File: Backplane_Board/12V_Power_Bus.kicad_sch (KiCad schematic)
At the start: 17 parts, among them U5 PKU3511SPI

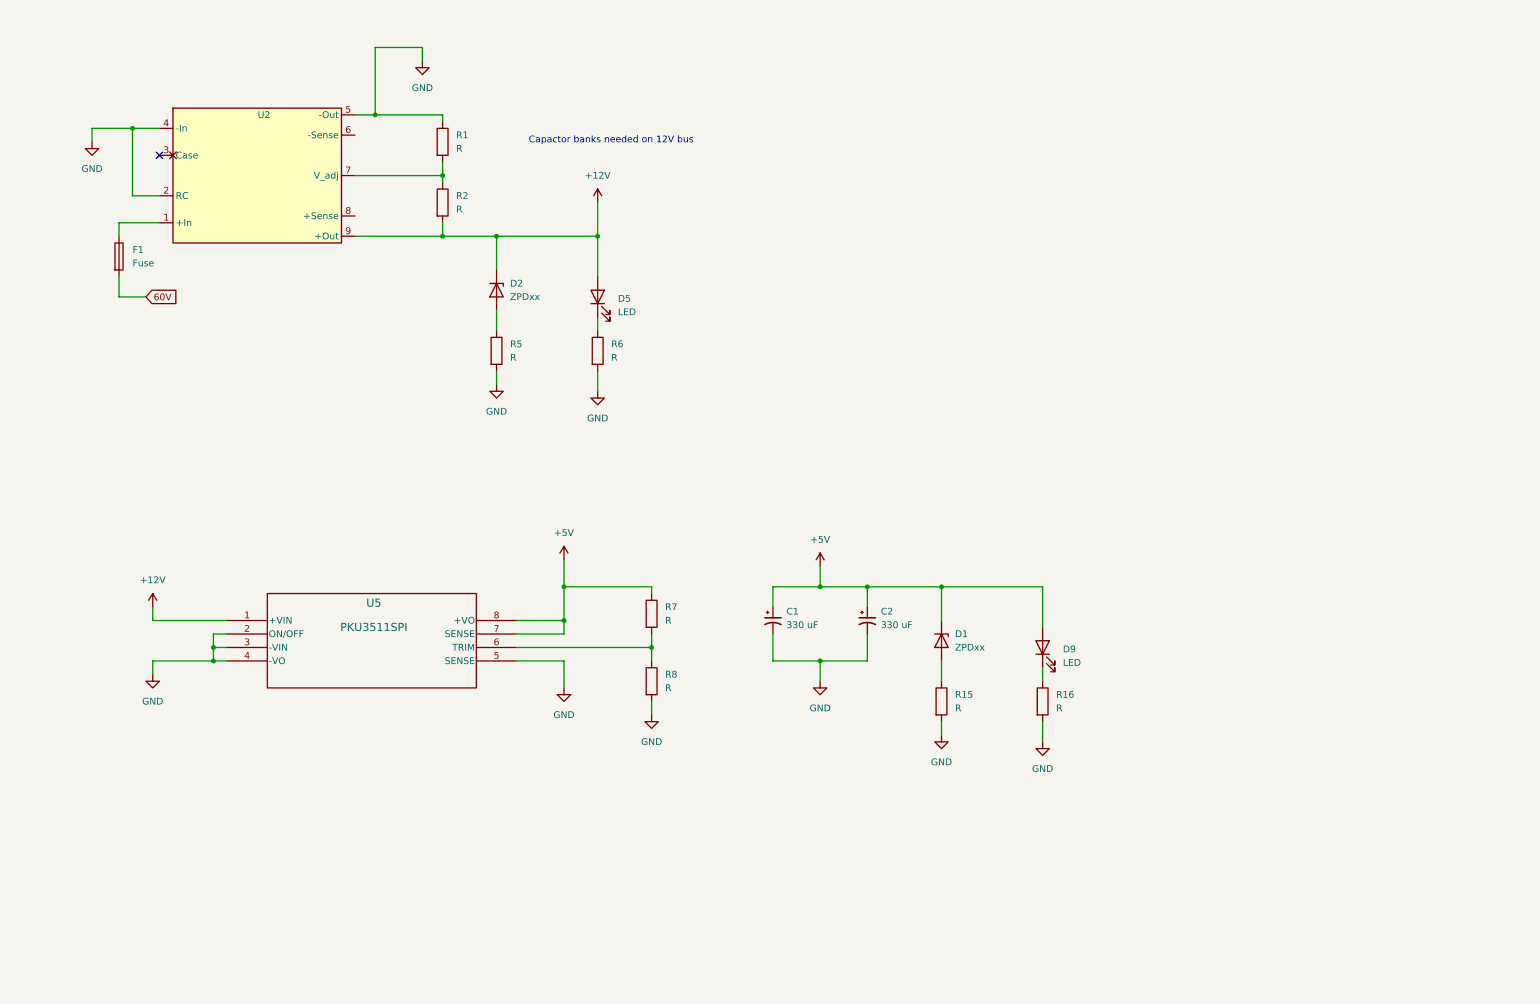
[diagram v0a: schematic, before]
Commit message: added ad converter
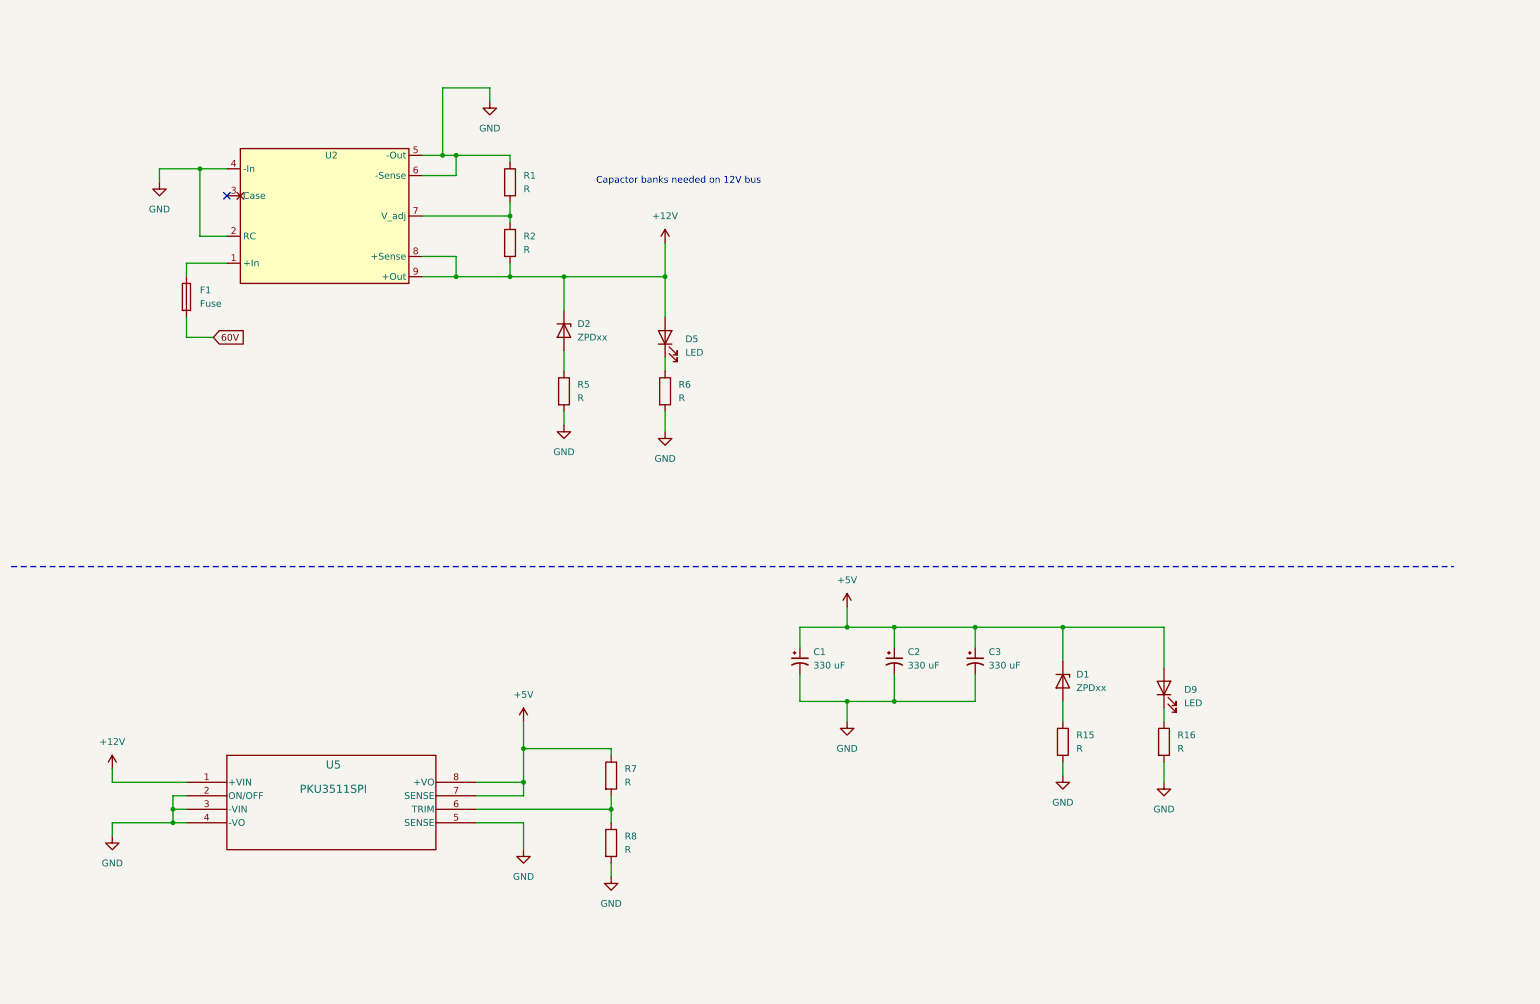
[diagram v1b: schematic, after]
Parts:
- added C3: 330 uF, 220UF CAP:CAP_16SVPG330MX, symbol Device:C_Polarized_Small_US
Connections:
- net +12V: now also U2.8 (+Sense)
- net +5V: now also C3.1
- net GND: now also U2.6 (-Sense), C3.2
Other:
- moved on the sheet: C1, C2, D1, D2, D5, D9, F1, R1, R15, R16, R2, R5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

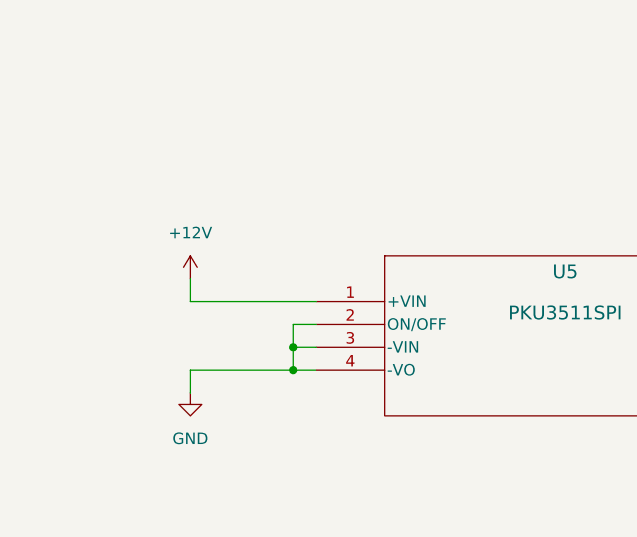
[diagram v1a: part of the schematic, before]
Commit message: add rerevised esc board and rough backplane schmatic
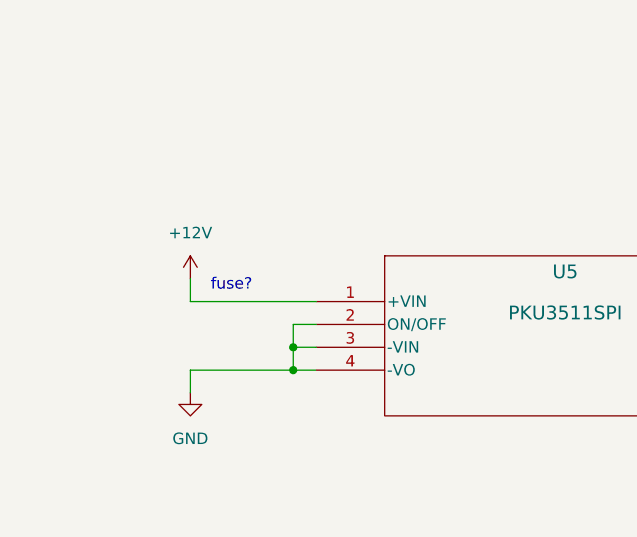
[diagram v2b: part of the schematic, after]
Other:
- note added: "fuse?"
- company: (none) -> Cabrillo Robtics
- title: (none) -> 5V and 12V Power Bus
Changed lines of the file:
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@@
 	(generator_version "8.0")
 	(paper "A4")
+	(title_block
+		(title "5V and 12V Power Bus")
+		(date "2024-09-30")
+		(rev "1")
+		(company "Cabrillo Robtics")
+		(comment 1 "LaserShark Backplane PCB")
+	)
 	(junction
 		(at 170.18 128.27)
@@
 			)
 		)
+	)
+	(text "fuse?"
+		(exclude_from_sim no)
+		(at 36.322 155.702 0)
+		(effects
+			(font
+				(size 1.27 1.27)
+				(color 255 53 95 1)
+			)
+		)

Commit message: backup before heavy revtion
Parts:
- removed D1, D2: ZPDxx, Diode_THT:D_DO-35_SOD27_P10.16mm_Horizontal, symbol Diode:ZPDxx
- removed R15, R5: R, symbol Device:R
- R1, R2: value R -> DNP
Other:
- note added: "The data sheet says: - recommended capactive load 3000uF on the output of this bus. - ESR is important and oppration is garented with a varafied ESR value greater than 5mOhm across the output conections - Should use both ceramic and electrostatic capactors"

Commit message: back plane board ready for review
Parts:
- removed U5: PKU3511SPI, PKU 3500S_FPM, symbol PKU3511SPI:PKU3511SPI
- added C20, C21, C22, C23: 22uF, C2012X5R1V226M125AC:CAPC2012X145N, symbol C2012X5R1V226M125AC:C2012X5R1V226M125AC
- added C24, C25, C26: 470 uF, 470UF CAP:CAP_EEHZU1V471V, symbol Device:C_Polarized_Small_US
- added C27, C28, C29: 0.1u, symbol Device:C_Polarized_Small_US
- added D4, D6: LED, symbol Device:LED
- added R18: 158k, symbol Device:R
- added R19, R20, R21, R22, R23, R24: R, symbol Device:R
- added U10, U7, U8, U9: SI7145DP-T1-GE3, SON8_SI7135DP-T1-GE3_VIS, symbol SI7145DP_T1_GE3:SI7145DP-T1-GE3
- added U5: LTC4418CUF-PBF, UF_20_ADI, symbol ul_LTC4418CUF-PBF:LTC4418CUF-PBF
- C1, C3: value 330 uF -> 0.1u; footprint 220UF CAP:CAP_16SVPG330MX -> (none)
- C2: value 330 uF -> 1n; footprint 220UF CAP:CAP_16SVPG330MX -> (none)
- R7, R8: value R -> 2.32k
- renumbered R6 to 10k
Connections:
- net +12V: now also C20.2, C21.2, C22.2, C23.2, C24.1, C25.1, C26.1, U10.5 (D), U10.6 (D), U10.7 (D), U10.8 (D), U5.15 (VOUT), U8.5 (D), U8.6 (D), U8.7 (D), U8.8 (D); no longer D5.2 (A), R2.2, U2.8 (+Sense), U2.9 (+Out)
- net +5V: now also R8.1; no longer C1.1, C2.1, C3.1, D9.2 (A)
- net GND: now also C20.1, C21.1, C22.1, C23.1, C24.2, C25.2, C26.2, C27.2, C28.2, C29.2, R18.2, R21.2, R24.2, U5.21 (GND), U5.8 (GND); no longer R8.2
- net at R7.2: now also D6.2 (A); no longer R8.1
- new net: C28.1, R19.1, U5.17 (V1)
- new net: C29.1, R22.1, U5.16 (V2)
- new net: C2.1, U5.1 (TMR)
- new net: D5.2 (A), R2.2, U2.8 (+Sense), U2.9 (+Out), U7.5 (D), U7.6 (D), U7.7 (D), U7.8 (D)
- new net: R18.1, U5.20 (HYS)
- new net: D4.2 (A), R8.2
- new net G1: U5.13 (G1), U7.4 (G), U8.4 (G)
- new net G2: U10.4 (G), U5.11 (G2), U9.4 (G)
- new net NIU: C1.1, U5.10 (INTVCC), U5.18 (EN), U5.19 (*SHDN)
- new net OV1: R20.2, R21.1, U5.3 (OV1)
- new net OV2: R23.2, R24.1, U5.5 (OV2)
- new net UV1: R19.2, R20.1, U5.2 (UV1)
- new net UV2: R22.2, R23.1, U5.4 (UV2)
- new net VALID1: D4.1 (K), U5.6 (*VALID1)
- new net VALID2: D6.1 (K), U5.7 (*VALID2)
- new net VS1: C3.1, U5.14 (VS1), U7.1 (S), U7.2 (S), U7.3 (S), U8.1 (S), U8.2 (S), U8.3 (S)
- new net VS2: C27.1, U10.1 (S), U10.2 (S), U10.3 (S), U5.12 (VS2), U9.1 (S), U9.2 (S), U9.3 (S)
- new net WALL_POWER: D9.2 (A), U9.5 (D), U9.6 (D), U9.7 (D), U9.8 (D)
- no-connect marks 1 -> 2
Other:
- note added: "12V Clean Power Bus"
- note added: "12V ESC Power Bus"
- note added: "Need to get the ESR of the caps to be over 5uF! Very static loading, so we could proably get away with even less capactance on this bus."
- note added: "P.8, HYS pulldown?"
- note removed: "Capactor banks needed on 12V bus"
- note removed: "The data sheet says: - recommended capactive load 3000uF on the output of this bus. - ESR is important and oppration is garented with a varafied ESR value greater than 5mOhm across the output conections - Should use both ceramic and electrostatic capactors"
- note removed: "fuse?"
- moved on the sheet: 10k, D5, F1, R1, R2, U2

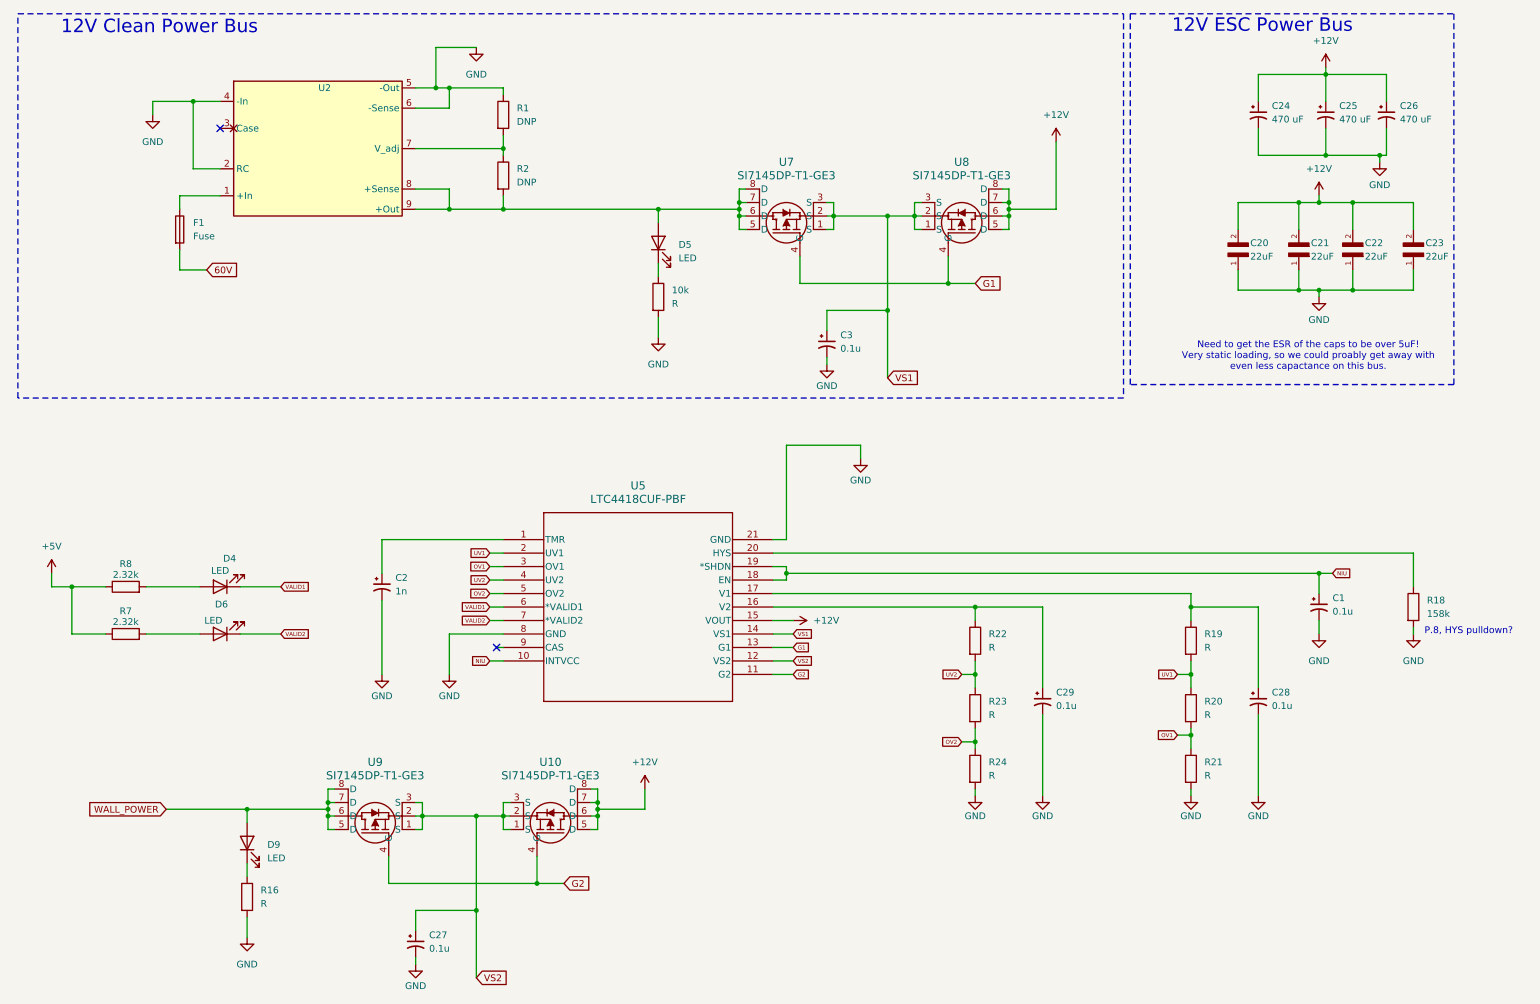
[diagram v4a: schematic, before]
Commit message: adding dull power path ic into sepret exption board
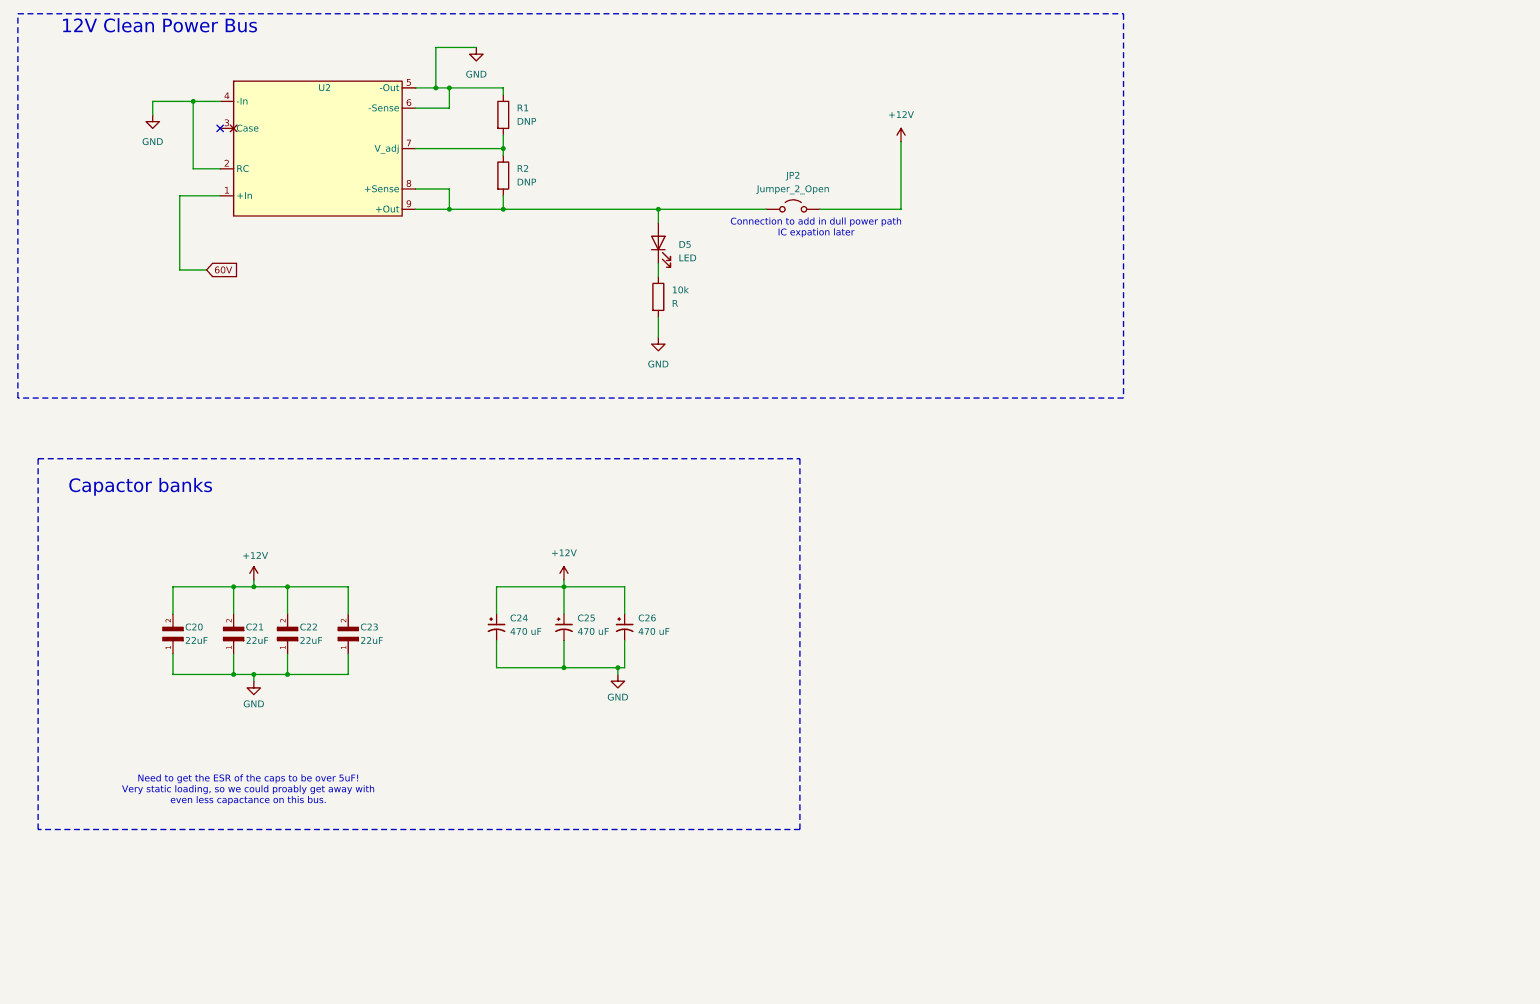
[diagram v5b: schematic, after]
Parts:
- removed C1, C27, C28, C29, C3: 0.1u, symbol Device:C_Polarized_Small_US
- removed C2: 1n, symbol Device:C_Polarized_Small_US
- removed D4, D6, D9: LED, symbol Device:LED
- removed F1: Fuse, symbol Device:Fuse
- removed R16, R19, R20, R21, R22, R23, R24: R, symbol Device:R
- removed R18: 158k, symbol Device:R
- removed R7, R8: 2.32k, symbol Device:R
- removed U10, U7, U8, U9: SI7145DP-T1-GE3, SON8_SI7135DP-T1-GE3_VIS, symbol SI7145DP_T1_GE3:SI7145DP-T1-GE3
- removed U5: LTC4418CUF-PBF, UF_20_ADI, symbol ul_LTC4418CUF-PBF:LTC4418CUF-PBF
- added JP2: Jumper_2_Open, symbol Jumper:Jumper_2_Open
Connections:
- net +12V: now also JP2.2 (B)
- net 60V: now also U2.1 (+In)
- net at D5.2 (A), R2.2, U2.8 (+Sense)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: now also JP2.1 (A)
- no-connect marks 2 -> 1
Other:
- note added: "Capactor banks"
- note added: "Connection to add in dull power path IC expation later"
- note removed: "12V ESC Power Bus"
- note removed: "P.8, HYS pulldown?"
- moved on the sheet: C20, C21, C22, C23, C24, C25, C26

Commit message: from desing review 1
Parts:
- removed C20, C21, C22, C23: 22uF, C2012X5R1V226M125AC:CAPC2012X145N, symbol C2012X5R1V226M125AC:C2012X5R1V226M125AC
- removed C24, C25, C26: 470 uF, 470UF CAP:CAP_EEHZU1V471V, symbol Device:C_Polarized_Small_US
- added C10, C12, C27, C29: 22uF, C2012X5R1V226M125AC:CAPC2012X145N, symbol C2012X5R1V226M125AC:C2012X5R1V226M125AC
- added C16, C17, C28: 680u, symbol Device:C_Polarized_Small_US
- added R18, R19, R20, R21: 330m, footprints:RES_KDV12_OHM-L, symbol Device:R_US
- R1, R2: now not fitted
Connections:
- net GND: now also C10.1, C12.1, C16.2, C17.2, C27.1, C28.2, C29.1
- new net: C29.2, R21.2
- new net: C10.2, R18.2
- new net: C12.2, R19.2
- new net: C27.2, R20.2
- new net 12V_ESC: C16.1, C17.1, C28.1, R18.1, R19.1, R20.1, R21.1
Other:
- note added: "- Same as the dynamic configuration that will be used with the motors. - Thinking of removing one of the 680u caps and shifing the resitors down accordingly. - We will have verey stedy current on this bus after the t=0+"
- note added: "Electrolytic"
- note removed: "Need to get the ESR of the caps to be over 5uF! Very static loading, so we could proably get away with even less capactance on this bus."
